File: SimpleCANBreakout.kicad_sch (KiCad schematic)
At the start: 17 parts, among them U1 TCAN332, U2 AMS1117-3.3

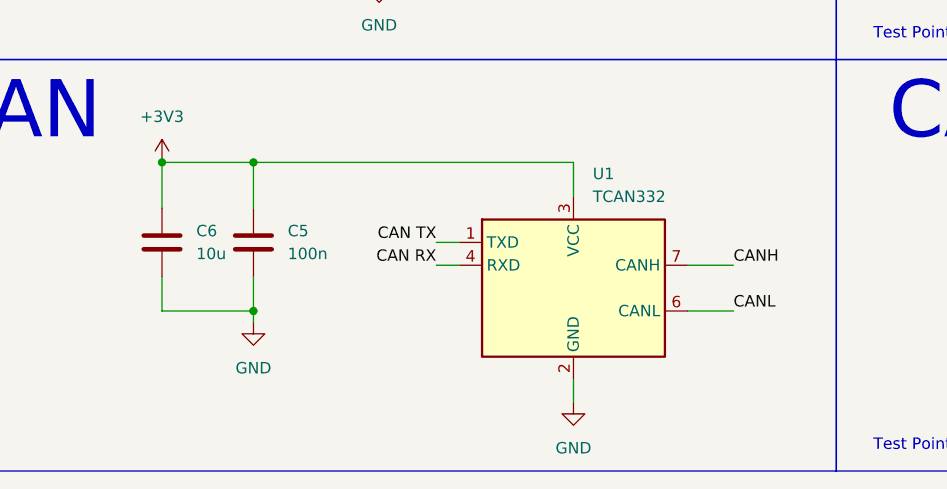
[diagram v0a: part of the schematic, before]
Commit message: Swap TCAN332 for SN65HVD230 and add LCSC part numbers
Rs (pin 8) is tied to GND through the existing pour for high-speed mode.
Production files regenerated with the Fabrication Toolkit.
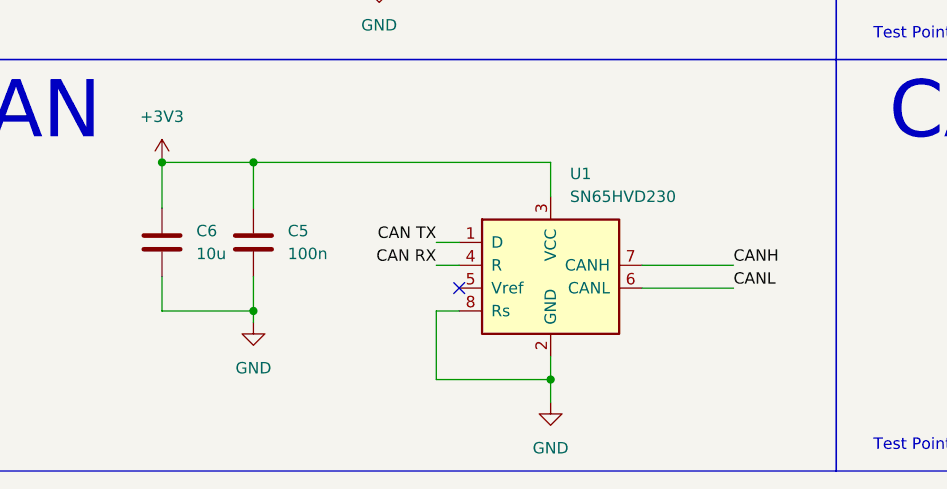
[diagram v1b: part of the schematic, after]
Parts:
- C1, C4, C6: LCSC Part (none) -> C19702
- C2, C3, C5: LCSC Part (none) -> C14663
- R1: LCSC Part (none) -> C22787
- U1: value TCAN332 -> SN65HVD230; symbol Interface_CAN_LIN:TCAN332 -> Interface_CAN_LIN:SN65HVD230; LCSC Part (none) -> C12084
- U2: LCSC Part (none) -> C6186
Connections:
- net GND: now also U1.8 (Rs)
- no-connect marks 0 -> 1
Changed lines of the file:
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@@
 	)
 	(symbol
-		(lib_id "Interface_CAN_LIN:TCAN332")
-		(at 83.82 83.82 0)
+		(lib_id "Interface_CAN_LIN:SN65HVD230")
+		(at 81.28 81.28 0)
 		(unit 1)
 		(body_style 1)
@@
 		(fields_autoplaced yes)
 		(property "Reference" "U1"
-			(at 85.9633 71.12 0)
-			(show_name no)
-			(do_not_autoplace no)
-			(effects
-				(font
-					(size 1.27 1.27)
-				)
-				(justify left)
-			)
-		)
-		(property "Value" "TCAN332"
-			(at 85.9633 73.66 0)
+			(at 83.4233 71.12 0)
+			(show_name no)
+			(do_not_autoplace no)
+			(effects
+				(font
+					(size 1.27 1.27)
+				)
+				(justify left)
+			)
+		)
+		(property "Value" "SN65HVD230"
+			(at 83.4233 73.66 0)
 			(show_name no)
 			(do_not_autoplace no)
@@
 		)
 		(property "Footprint" "Package_SO:SOIC-8_3.9x4.9mm_P1.27mm"
-			(at 83.82 96.52 0)
-			(hide yes)
-			(show_name no)
-			(do_not_autoplace no)
-			(effects
-				(font
-					(size 1.27 1.27)
-					(italic yes)
-				)
-			)
-		)
-		(property "Datasheet" "http://www.ti.com/lit/ds/symlink/tcan337.pdf"
-			(at 83.82 83.82 0)
-			(hide yes)
-			(show_name no)
-			(do_not_autoplace no)
-			(effects
-				(font
-					(size 1.27 1.27)
-				)
-			)
-		)
-		(property "Description" "High-Speed CAN Transceiver, 1Mbps, 3.3V supply, SOT-23-8/SOIC-8"
-			(at 83.82 83.82 0)
-			(hide yes)
-			(show_name no)
-			(do_not_autoplace no)
-			(effects
-				(font
-					(size 1.27 1.27)
-				)
-			)
+			(at 81.28 93.98 0)
+			(hide yes)
+			(show_name no)
+			(do_not_autoplace no)
+			(effects
+				(font
+					(size 1.27 1.27)
+				)
+			)
+		)
+		(property "Datasheet" "http://www.ti.com/lit/ds/symlink/sn65hvd230.pdf"
+			(at 78.74 71.12 0)
+			(hide yes)
+			(show_name no)
+			(do_not_autoplace no)
+			(effects
+				(font
+					(size 1.27 1.27)
+				)
+			)
+		)
+		(property "Description" "CAN Bus Transceivers, 3.3V, 1Mbps, Low-Power capabilities, SOIC-8"
+			(at 81.28 81.28 0)
+			(hide yes)
+			(show_name no)
+			(do_not_autoplace no)
+			(effects
+				(font
+					(size 1.27 1.27)
+				)
+			)
+		)
+		(property "LCSC Part" "C12084"
+			(at 81.28 81.28 0)
+			(hide yes)
+			(show_name no)
+			(do_not_autoplace no)
+			(effects
+				(font
+					(size 1.27 1.27)
+				)
+			)
+		)
+		(pin "5"
+		)
+		(pin "8"
+		)
+		(pin "3"
 		)
 		(pin "6"
 		)
-		(pin "3"
+		(pin "2"
 		)
 		(pin "4"
 		)
-		(pin "2"
-		)
-		(pin "5"
+		(pin "7"
 		)
 		(pin "1"
-		)
-		(pin "8"
-		)
-		(pin "7"
 		)
 		(instances
@@
 	(symbol
 		(lib_id "power:GND")
-		(at 83.82 96.52 0)
+		(at 81.28 96.52 0)
 		(unit 1)
 		(body_style 1)
@@
 		(fields_autoplaced yes)
 		(property "Reference" "#PWR06"
-			(at 83.82 102.87 0)
+			(at 81.28 102.87 0)
 			(hide yes)
 			(show_name no)
@@
 		)
 		(property "Value" "GND"
-			(at 83.82 101.6 0)
+			(at 81.28 101.6 0)
 			(show_name no)
 			(do_not_autoplace no)
@@
 		)
 		(property "Footprint" ""
-			(at 83.82 96.52 0)
+			(at 81.28 96.52 0)
 			(hide yes)
 			(show_name no)
@@
 		)
 		(property "Datasheet" ""
-			(at 83.82 96.52 0)
+			(at 81.28 96.52 0)
 			(hide yes)
 			(show_name no)
@@
 		)
 		(property "Description" "Power symbol creates a global label with name \"GND\" , ground"
-			(at 83.82 96.52 0)
+			(at 81.28 96.52 0)
 			(hide yes)
 			(show_name no)
@@
 			)
 		)
+		(property "LCSC Part" "C19702"
+			(at 38.1 78.74 0)
+			(hide yes)
+			(show_name no)
+			(do_not_autoplace no)
+			(effects
+				(font
+					(size 1.27 1.27)
+				)
+			)
+		)
 		(pin "1"
 		)
@@
 			)
 		)
+		(property "LCSC Part" "C22787"
+			(at 200.66 80.01 0)
+			(hide yes)
+			(show_name no)
+			(do_not_autoplace no)
+			(effects
+				(font
+					(size 1.27 1.27)
+				)
+			)
+		)
 		(pin "2"
 		)
@@
 			)
 		)
+		(property "LCSC Part" "C19702"
+			(at 36.83 40.64 0)
+			(hide yes)
+			(show_name no)
+			(do_not_autoplace no)
+			(effects
+				(font
+					(size 1.27 1.27)
+				)
+			)
+		)
 		(pin "1"
 		)
@@
 			)
 		)
+		(property "LCSC Part" "C14663"
+			(at 46.99 40.64 0)
+			(hide yes)
+			(show_name no)
+			(do_not_autoplace no)
+			(effects
+				(font
+					(size 1.27 1.27)
+				)
+			)
+		)
 		(pin "1"
 		)
@@
 			)
 		)
+		(property "LCSC Part" "C6186"
+			(at 62.23 33.02 0)
+			(hide yes)
+			(show_name no)
+			(do_not_autoplace no)
+			(effects
+				(font
+					(size 1.27 1.27)
+				)
+			)
+		)
 		(pin "2"
 		)
@@
 			)
 		)
+		(property "LCSC Part" "C14663"
+			(at 48.26 78.74 0)
+			(hide yes)
+			(show_name no)
+			(do_not_autoplace no)
+			(effects
+				(font
+					(size 1.27 1.27)
+				)
+			)
+		)
 		(pin "1"
 		)
@@
 			)
 		)
+		(property "LCSC Part" "C19702"
+			(at 86.36 40.64 0)
+			(hide yes)
+			(show_name no)
+			(do_not_autoplace no)
+			(effects
+				(font
+					(size 1.27 1.27)
+				)
+			)
+		)
 		(pin "1"
 		)
@@
 			)
 		)
+		(property "LCSC Part" "C14663"
+			(at 73.66 40.64 0)
+			(hide yes)
+			(show_name no)
+			(do_not_autoplace no)
+			(effects
+				(font
+					(size 1.27 1.27)
+				)
+			)
+		)
 		(pin "1"
 		)
@@
 	(wire
 		(pts
-			(xy 38.1 69.85) (xy 83.82 69.85)
-		)
-		(stroke
-			(width 0)
-			(type default)
-		)
-	)
-	(wire
-		(pts
-			(xy 83.82 69.85) (xy 83.82 73.66)
+			(xy 38.1 69.85) (xy 81.28 69.85)
+		)
+		(stroke
+			(width 0)
+			(type default)
+		)
+	)
+	(wire
+		(pts
+			(xy 81.28 69.85) (xy 81.28 73.66)
 		)
 		(stroke
@@
 	(wire
 		(pts
-			(xy 83.82 93.98) (xy 83.82 96.52)
+			(xy 81.28 91.44) (xy 81.28 96.52)
 		)
 		(stroke
@@
 	(wire
 		(pts
-			(xy 96.52 81.28) (xy 101.6 81.28)
-		)
-		(stroke
-			(width 0)
-			(type default)
-		)
-	)
-	(wire
-		(pts
-			(xy 96.52 86.36) (xy 101.6 86.36)
+			(xy 91.44 81.28) (xy 101.6 81.28)
+		)
+		(stroke
+			(width 0)
+			(type default)
+		)
+	)
+	(wire
+		(pts
+			(xy 91.44 83.82) (xy 101.6 83.82)
 		)
 		(stroke
@@
 	)
 	(label "CANL"
-		(at 101.6 86.36 0)
+		(at 101.6 83.82 0)
 		(effects
 			(font
@@
 		)
 	)
+	(wire
+		(pts
+			(xy 71.12 86.36) (xy 68.58 86.36)
+		)
+		(stroke
+			(width 0)
+			(type default)
+		)
+	)
+	(wire
+		(pts
+			(xy 68.58 86.36) (xy 68.58 93.98)
+		)
+		(stroke
+			(width 0)
+			(type default)
+		)
+	)
+	(wire
+		(pts
+			(xy 68.58 93.98) (xy 81.28 93.98)
+		)
+		(stroke
+			(width 0)
+			(type default)
+		)
+	)
+	(junction
+		(at 81.28 93.98)
+		(diameter 0)
+		(color 0 0 0 0)
+	)
+	(no_connect
+		(at 71.12 83.82)
+	)
 	(sheet_instances

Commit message: Schematic title block (title, date, rev 1.0); PDF re-exported
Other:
- title: (none) -> SimpleCANBreakout
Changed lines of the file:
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@@
 	(generator_version "10.0")
 	(paper "A4")
+	(title_block
+		(title "SimpleCANBreakout")
+		(date "2026-10-17")
+		(rev "1.0")
+	)
 	(junction
 		(at 73.66 48.26)
